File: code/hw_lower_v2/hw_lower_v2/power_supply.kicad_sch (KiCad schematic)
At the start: 0 parts

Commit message: further lower board sch work
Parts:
- added C14, C15, C18: 10u, symbol Device:C_Polarized
- added C16, C19: 100u, symbol Device:C_Polarized
- added C17: 100n 25V, symbol Device:C
- added D3, D4, D5: LED, Diode_SMD:D_0603_1608Metric, symbol Device:LED
- added PS1: HLK-5M12, Converter_ACDC:Converter_ACDC_Hi-Link_HLK-5Mxx, symbol Converter_ACDC:HLK-5M12
- added R34, R35, R36, R37: DNP, Resistor_SMD:R_0603_1608Metric, symbol Device:R
- added R38: 510, Resistor_SMD:R_0603_1608Metric, symbol Device:R
- added R39: 160, Resistor_SMD:R_0603_1608Metric, symbol Device:R
- added R40: 75, Resistor_SMD:R_0603_1608Metric, symbol Device:R
- added U5, U6: AMS1117, Package_TO_SOT_SMD:SOT-223-3_TabPin2, symbol Regulator_Linear:AMS1117
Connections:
- net L_in: now also PS1.1 (AC/L)
- net N_in: now also PS1.2 (AC/N)
- new net: D4.1 (K), R39.1
- new net: R34.1, R35.2, U5.1 (ADJ)
- new net: D3.1 (K), R38.1
- new net: D5.1 (K), R40.1
- new net: R36.1, R37.2, U6.1 (ADJ)
- new net +12V: C14.1, C15.1, C17.1, C18.1, D4.2 (A), PS1.4 (+Vout), U5.3 (VI), U6.3 (VI)
- new net +3.3V: C16.1, D5.2 (A), R34.2, U5.2 (VO)
- new net +5V: C19.1, D3.2 (A), R36.2, U6.2 (VO)
- new net GND: C14.2, C15.2, C16.2, C17.2, C18.2, C19.2, PS1.3 (-Vout), R35.1, R37.1, R38.2, R39.2, R40.2
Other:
- note added: "line overvoltage protection MOS?"

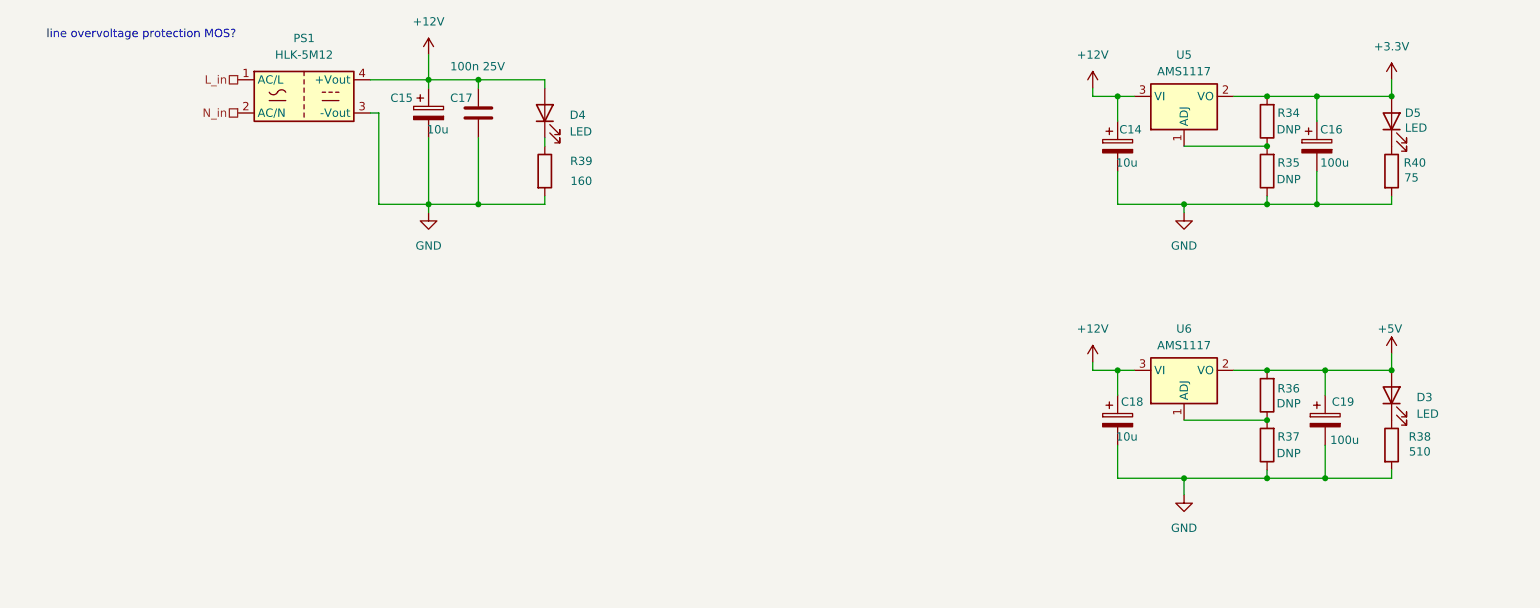
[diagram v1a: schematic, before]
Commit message: add 12V voltage inverter and polish
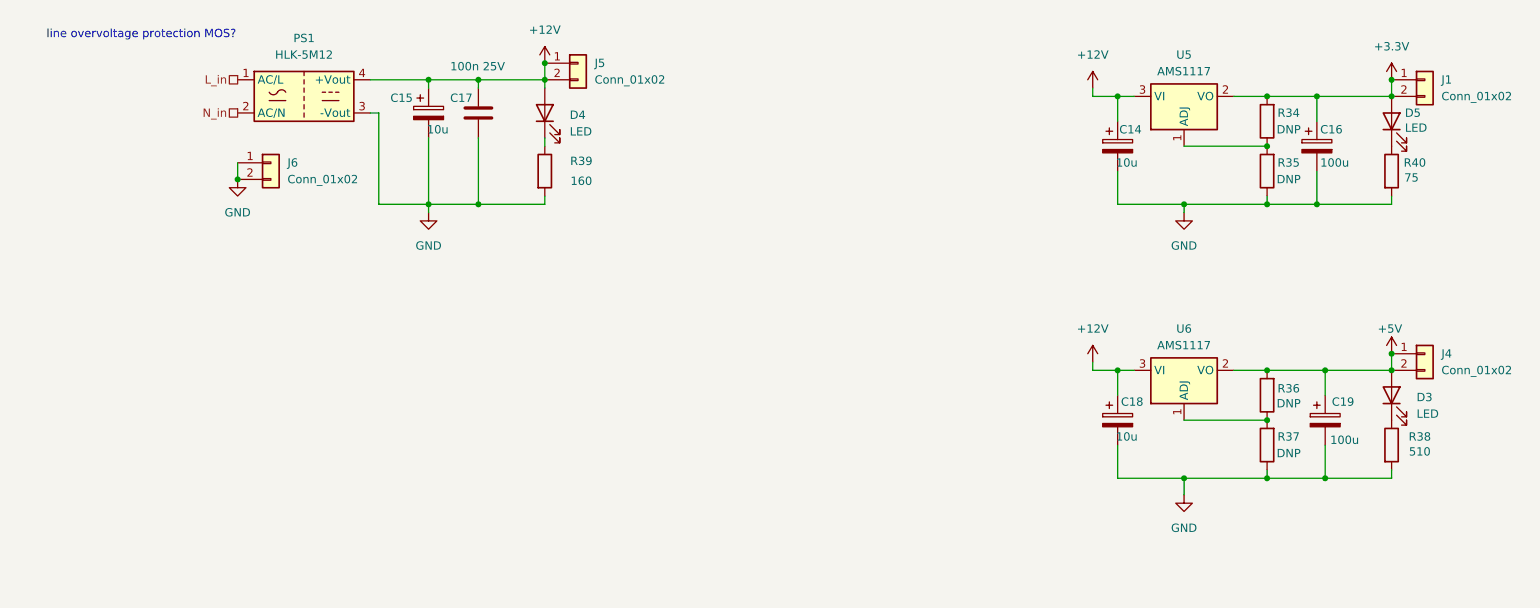
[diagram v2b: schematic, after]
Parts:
- added J1, J4, J5, J6: Conn_01x02, symbol Connector_Generic:Conn_01x02
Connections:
- net +12V: now also J5.1 (Pin_1), J5.2 (Pin_2)
- net +3.3V: now also J1.1 (Pin_1), J1.2 (Pin_2)
- net +5V: now also J4.1 (Pin_1), J4.2 (Pin_2)
- net GND: now also J6.1 (Pin_1), J6.2 (Pin_2)

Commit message: schematic is done
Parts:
- added C20, C21: 10u, symbol Device:C_Polarized
- added C9: 0.1uF/275Vac, symbol Device:C
- added F1: 1A, symbol Device:Fuse
- added FL1: Filter_EMI_CommonMode, symbol Device:Filter_EMI_CommonMode
- added J7, J8: Conn_01x02, symbol Connector_Generic:Conn_01x02
- added RV1: 10D561K, symbol Device:Varistor
- added U7: ICL7660A, symbol multi_new:ICL7660A
- C17: value 100n 25V -> 100n; footprint (none) -> Capacitor_SMD:C_0805_2012Metric
- PS1: JLCPCB Part # (none) -> C2923575
- R34: value DNP -> 75R
- R35, R37: value DNP -> 120R
- R36: value DNP -> 39R
- R38: value 510 -> 510R
- R39: value 160 -> 160R
- R40: value 75 -> 75R
- U5, U6: JLCPCB Part # (none) -> C347224
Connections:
- net +12V: now also J8.1 (Pin_1), J8.2 (Pin_2), U7.8 (V+)
- net GND: now also C21.1, U7.3 (GND)
- net L_in: now also F1.1; no longer PS1.1 (AC/L)
- net N_in: now also C9.2, FL1.3, RV1.2; no longer PS1.2 (AC/N)
- new net: C20.1, U7.2 (CAP+)
- new net: C20.2, U7.4 (CAP-)
- new net: C9.1, F1.2, FL1.1, RV1.1
- new net: FL1.2, PS1.1 (AC/L)
- new net: FL1.4, PS1.2 (AC/N)
- new net -12V: C21.2, J7.1 (Pin_1), J7.2 (Pin_2), U7.5 (VOUT)
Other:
- note removed: "line overvoltage protection MOS?"
- moved on the sheet: C15, C17, D4, J5, J6, PS1, R39

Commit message: finishing up sch and creating footprints
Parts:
- renumbered C9 to C12, C15 to C13, C17 to C14, C20 to C15, C21 to C16, C14 to C17, C16 to C19, C19 to C20, D3 to D6, J8 to J10, J5 to J11, J7 to J12, J1 to J13, J4 to J14, J6 to J9, R39 to R37, R34 to R38, R35 to R39, R36 to R40, R37 to R41, R40 to R42, R38 to R43, U7 to U5, U5 to U6, U6 to U7

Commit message: wip
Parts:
- C12: JLCPCB Part # C914484 -> (none); LCSC (none) -> C914484
- PS1: JLCPCB Part # C2923575 -> (none); LCSC (none) -> C2923575
- RV1: JLCPCB Part # C2761663 -> (none); LCSC (none) -> C2761663
- U5: JLCPCB Part # C7881 -> (none); LCSC (none) -> C7881
- U6, U7: JLCPCB Part # C347224 -> (none); LCSC (none) -> C347224

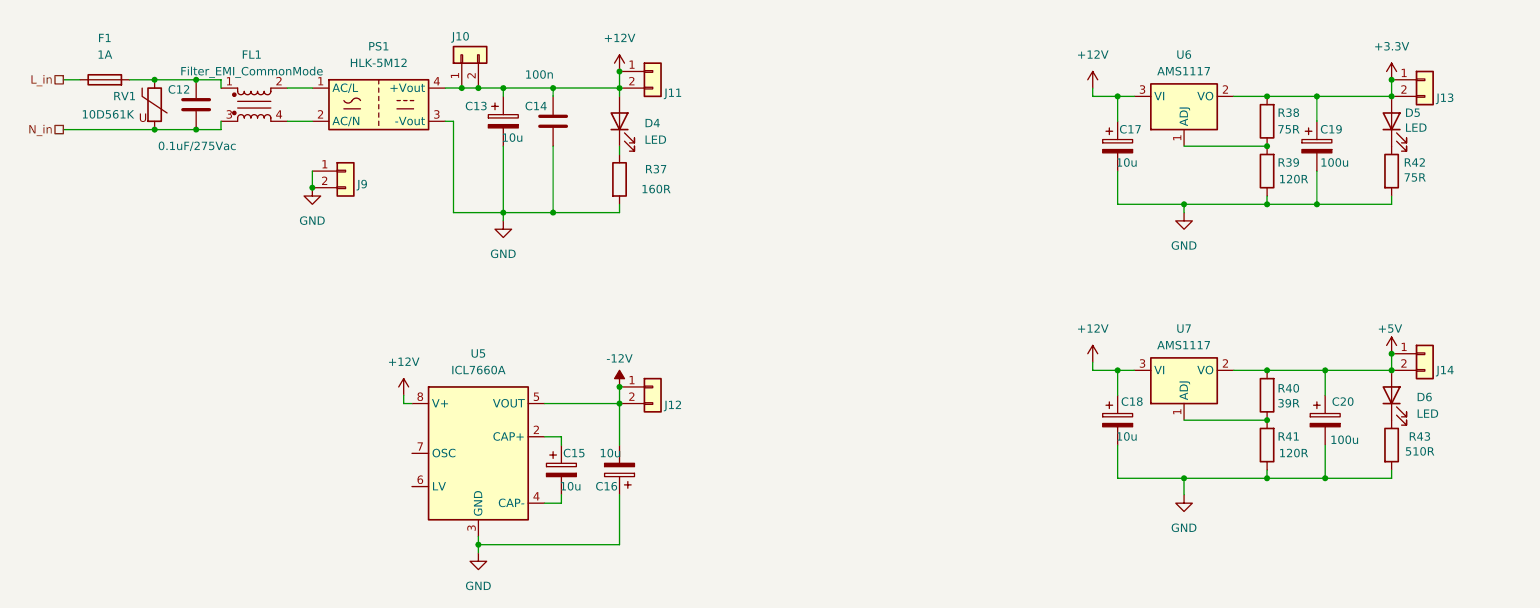
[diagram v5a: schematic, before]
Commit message: finished schematic, started first pass of layout
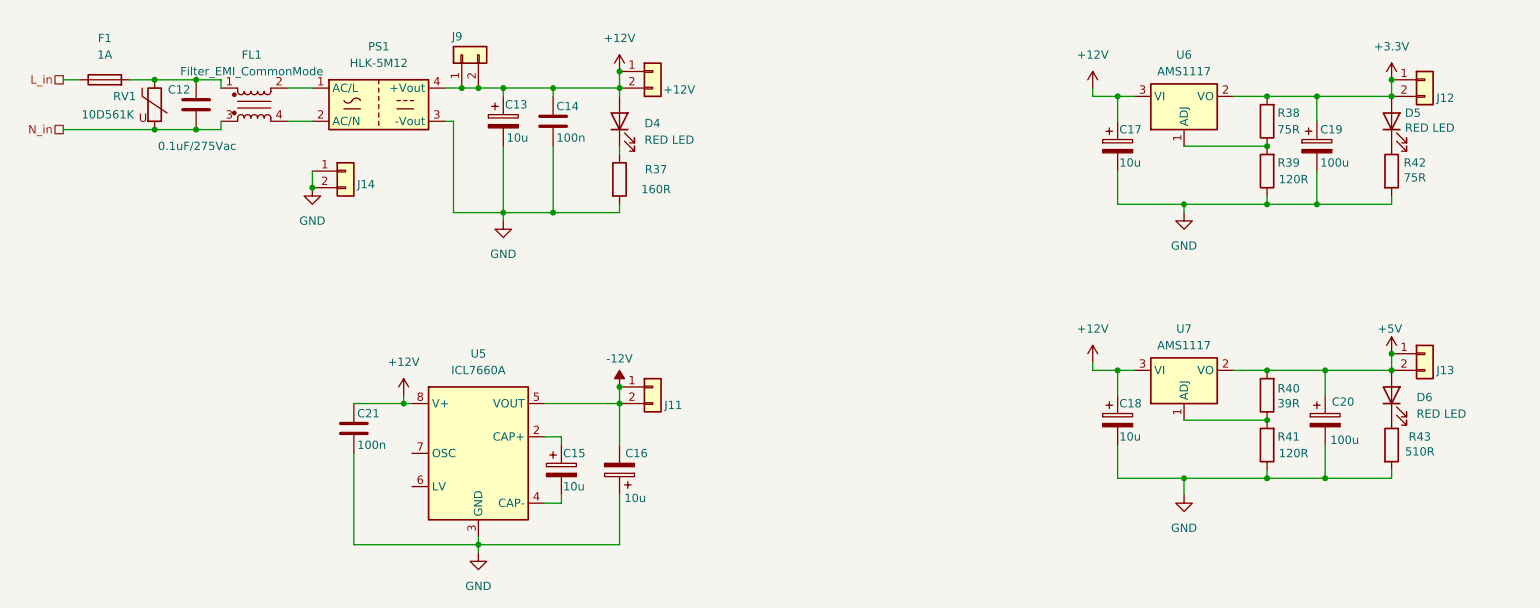
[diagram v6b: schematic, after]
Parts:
- added C21: 100n, Capacitor_SMD:C_0805_2012Metric, symbol Device:C
- C12: footprint (none) -> JLCPCB:CAP-TH_L18.0-W7.0-P15.00-D0.7
- C13, C15, C16, C17, C18: value 10u -> 10u; footprint (none) -> Capacitor_SMD:CP_Elec_4x5.4; LCSC (none) -> C72485
- C14: LCSC (none) -> C38141
- C19, C20: footprint (none) -> Capacitor_SMD:CP_Elec_6.3x5.4; LCSC (none) -> C5138965
- D4, D5, D6: value LED -> RED LED; LCSC (none) -> C7496820
- F1: footprint (none) -> JLCPCB:F1206; LCSC (none) -> C910830
- FL1: footprint (none) -> JLCPCB:FILTER-TH_4P-L17.0-W12.0-P7.00-D0.6-S8.00; LCSC (none) -> C126488
- J10: renamed from J11; footprint (none) -> Connector_PinHeader_2.54mm:PinHeader_1x02_P2.54mm_Vertical; Name (none) -> +12V
- J11: renamed from J12; footprint (none) -> Connector_PinHeader_2.54mm:PinHeader_1x02_P2.54mm_Vertical
- J12: renamed from J13; footprint (none) -> Connector_PinHeader_2.54mm:PinHeader_1x02_P2.54mm_Vertical
- J13: renamed from J14; footprint (none) -> Connector_PinHeader_2.54mm:PinHeader_1x02_P2.54mm_Vertical
- J14: renamed from J9; footprint (none) -> Connector_PinHeader_2.54mm:PinHeader_1x02_P2.54mm_Vertical
- J9: renamed from J10; footprint (none) -> Connector_PinHeader_2.54mm:PinHeader_1x02_P2.54mm_Vertical
- R37: LCSC (none) -> C22814
- R38, R42: LCSC (none) -> C112309
- R39, R41: LCSC (none) -> C125925
- R40: LCSC (none) -> C137733
- R43: LCSC (none) -> C23193
- RV1: footprint (none) -> JLCPCB:RES-TH_L12.5-W4.4-P7.50-D0.8-S3.60
- U5: footprint (none) -> JLCPCB:SOIC-8_L5.0-W4.0-P1.27-LS6.0-BL
- U6, U7: footprint Package_TO_SOT_SMD:SOT-223-3_TabPin2 -> JLCPCB:SOT-223_L6.7-W3.5-P2.30-BR
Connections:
- net +12V: now also C21.1
- net GND: now also C21.2

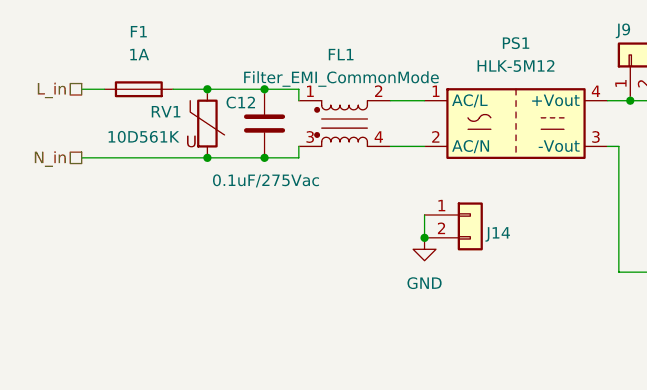
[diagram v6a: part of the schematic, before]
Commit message: Preliminary pcb component placement done
PCB size currently is around 100mm X 100mm with the mezanine board being ~40mm x 100mm
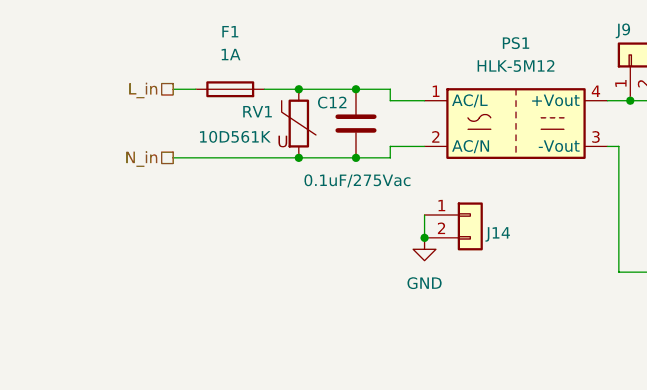
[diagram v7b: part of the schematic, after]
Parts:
- removed FL1: Filter_EMI_CommonMode, JLCPCB:FILTER-TH_4P-L17.0-W12.0-P7.00-D0.6-S8.00, symbol Device:Filter_EMI_CommonMode
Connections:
- net N_in: now also PS1.2 (AC/N)
- net at C12.1, F1.2, RV1.1: now also PS1.1 (AC/L)
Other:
- moved on the sheet: C12, F1, RV1
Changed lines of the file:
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@@
 	)
 	(junction
-		(at 54.61 39.37)
+		(at 64.77 39.37)
 		(diameter 0)
 		(color 0 0 0 0)
@@
 	)
 	(junction
-		(at 48.26 46.99)
+		(at 58.42 46.99)
 		(diameter 0)
 		(color 0 0 0 0)
 	)
 	(junction
-		(at 54.61 46.99)
+		(at 64.77 46.99)
 		(diameter 0)
 		(color 0 0 0 0)
 	)
 	(junction
-		(at 48.26 39.37)
+		(at 58.42 39.37)
 		(diameter 0)
 		(color 0 0 0 0)
@@
 	(wire
 		(pts
-			(xy 58.42 45.72) (xy 58.42 46.99)
+			(xy 68.58 45.72) (xy 68.58 46.99)
 		)
 		(stroke
@@
 	(wire
 		(pts
-			(xy 34.29 39.37) (xy 36.83 39.37)
+			(xy 44.45 39.37) (xy 46.99 39.37)
 		)
 		(stroke
@@
 	(wire
 		(pts
-			(xy 58.42 40.64) (xy 58.42 39.37)
+			(xy 68.58 40.64) (xy 68.58 39.37)
 		)
 		(stroke
@@
 	(wire
 		(pts
-			(xy 54.61 46.99) (xy 58.42 46.99)
+			(xy 64.77 46.99) (xy 68.58 46.99)
 		)
 		(stroke
@@
 	(wire
 		(pts
-			(xy 48.26 46.99) (xy 54.61 46.99)
+			(xy 58.42 46.99) (xy 64.77 46.99)
 		)
 		(stroke
@@
 	(wire
 		(pts
-			(xy 44.45 39.37) (xy 48.26 39.37)
+			(xy 54.61 39.37) (xy 58.42 39.37)
 		)
 		(stroke
@@
 	(wire
 		(pts
-			(xy 34.29 46.99) (xy 48.26 46.99)
+			(xy 44.45 46.99) (xy 58.42 46.99)
 		)
 		(stroke
@@
 	(wire
 		(pts
-			(xy 54.61 39.37) (xy 58.42 39.37)
+			(xy 64.77 39.37) (xy 68.58 39.37)
 		)
 		(stroke
@@
 	(wire
 		(pts
-			(xy 48.26 39.37) (xy 54.61 39.37)
+			(xy 58.42 39.37) (xy 64.77 39.37)
 		)
 		(stroke
@@
 	(hierarchical_label "N_in"
 		(shape passive)
-		(at 34.29 46.99 180)
+		(at 44.45 46.99 180)
 		(fields_autoplaced yes)
 		(effects
@@
 	(hierarchical_label "L_in"
 		(shape passive)
-		(at 34.29 39.37 180)
+		(at 44.45 39.37 180)
 		(fields_autoplaced yes)
 		(effects
@@
 	(symbol
 		(lib_id "Device:C")
-		(at 54.61 43.18 0)
+		(at 64.77 43.18 0)
 		(unit 1)
 		(exclude_from_sim no)
@@
 		(dnp no)
 		(property "Reference" "C12"
-			(at 50.292 40.894 0)
+			(at 60.452 40.894 0)
 			(effects
 				(font
@@
 		)
 		(property "Value" "0.1uF/275Vac"
-			(at 48.768 49.53 0)
+			(at 58.928 49.53 0)
 			(effects
 				(font
@@
 		)
 		(property "Footprint" "JLCPCB:CAP-TH_L18.0-W7.0-P15.00-D0.7"
-			(at 55.5752 46.99 0)
+			(at 65.7352 46.99 0)
 			(effects
 				(font
@@
 		)
 		(property "Datasheet" "~"
-			(at 54.61 43.18 0)
+			(at 64.77 43.18 0)
 			(effects
 				(font
@@
 		)
 		(property "Description" "Unpolarized capacitor"
-			(at 54.61 43.18 0)
+			(at 64.77 43.18 0)
 			(effects
 				(font
@@
 		)
 		(property "LCSC" "C914484"
-			(at 54.61 43.18 0)
+			(at 64.77 43.18 0)
 			(effects
 				(font
@@
 	(symbol
 		(lib_id "Device:Fuse")
-		(at 40.64 39.37 90)
+		(at 50.8 39.37 90)
 		(unit 1)
 		(exclude_from_sim no)
@@
 		(fields_autoplaced yes)
 		(property "Reference" "F1"
-			(at 40.64 33.02 90)
+			(at 50.8 33.02 90)
 			(effects
 				(font
@@
 		)
 		(property "Value" "1A"
-			(at 40.64 35.56 90)
+			(at 50.8 35.56 90)
 			(effects
 				(font
@@
 		)
 		(property "Footprint" "JLCPCB:F1206"
-			(at 40.64 41.148 90)
+			(at 50.8 41.148 90)
 			(effects
 				(font
@@
 		)
 		(property "Datasheet" "~"
-			(at 40.64 39.37 0)
+			(at 50.8 39.37 0)
 			(effects
 				(font
@@
 		)
 		(property "Description" "Fuse"
-			(at 40.64 39.37 0)
+			(at 50.8 39.37 0)
 			(effects
 				(font
@@
 		)
 		(property "LCSC" "C910830"
-			(at 40.64 39.37 0)
+			(at 50.8 39.37 0)
 			(effects
 				(font
@@
 	(symbol
 		(lib_id "Device:Varistor")
-		(at 48.26 43.18 0)
+		(at 58.42 43.18 0)
 		(unit 1)
 		(exclude_from_sim no)
@@
 		(dnp no)
 		(property "Reference" "RV1"
-			(at 41.91 41.91 0)
+			(at 52.07 41.91 0)
 			(effects
 				(font
@@
 		)
 		(property "Value" "10D561K"
-			(at 37.084 44.704 0)
+			(at 47.244 44.704 0)
 			(effects
 				(font
@@
 		)
 		(property "Footprint" "JLCPCB:RES-TH_L12.5-W4.4-P7.50-D0.8-S3.60"
-			(at 46.482 43.18 90)
+			(at 56.642 43.18 90)
 			(effects
 				(font
@@
 		)
 		(property "Datasheet" "~"
-			(at 48.26 43.18 0)
+			(at 58.42 43.18 0)
 			(effects
 				(font
@@
 		)
 		(property "Description" "Voltage dependent resistor"
-			(at 48.26 43.18 0)
+			(at 58.42 43.18 0)
 			(effects
 				(font
@@
 		)
 		(property "Sim.Name" "kicad_builtin_varistor"
-			(at 48.26 43.18 0)
+			(at 58.42 43.18 0)
 			(effects
 				(font
@@
 		)
 		(property "Sim.Device" "SUBCKT"
-			(at 48.26 43.18 0)
+			(at 58.42 43.18 0)
 			(effects
 				(font
@@
 		)
 		(property "Sim.Pins" "1=A 2=B"
-			(at 48.26 43.18 0)
+			(at 58.42 43.18 0)
 			(effects
 				(font
@@
 		)
 		(property "Sim.Params" "threshold=1k"
-			(at 48.26 43.18 0)
+			(at 58.42 43.18 0)
 			(effects
 				(font
@@
 		)
 		(property "Sim.Library" "${KICAD7_SYMBOL_DIR}/Simulation_SPICE.sp"
-			(at 48.26 43.18 0)
+			(at 58.42 43.18 0)
 			(effects
 				(font
@@
 		)
 		(property "LCSC" "C2761663"
-			(at 48.26 43.18 0)
+			(at 58.42 43.18 0)
 			(effects
 				(font
@@
 					(unit 1)
 				)
-			)
-		)
-	)
-	(symbol
-		(lib_id "Device:Filter_EMI_CommonMode")
-		(at 63.5 43.18 0)
-		(unit 1)
-		(exclude_from_sim no)
-		(in_bom yes)
-		(on_board yes)
-		(dnp no)
-		(fields_autoplaced yes)
-		(property "Reference" "FL1"
-			(at 63.119 35.56 0)
-			(effects
-				(font
-					(size 1.27 1.27)
-				)
-			)
-		)
-		(property "Value" "Filter_EMI_CommonMode"
-			(at 63.119 38.1 0)
-			(effects
-				(font
-					(size 1.27 1.27)
-				)
-			)
-		)
-		(property "Footprint" "JLCPCB:FILTER-TH_4P-L17.0-W12.0-P7.00-D0.6-S8.00"
-			(at 63.5 42.164 0)
-			(effects
-				(font
-					(size 1.27 1.27)
-				)
-				(hide yes)
-			)
-		)
-		(property "Datasheet" "~"
-			(at 63.5 42.164 0)
-			(effects
-				(font
-					(size 1.27 1.27)
-				)
-				(hide yes)
-			)
-		)
-		(property "Description" "EMI 2-inductor common mode filter"
-			(at 63.5 43.18 0)
-			(effects
-				(font
-					(size 1.27 1.27)
-				)
-				(hide yes)
-			)
-		)
-		(property "LCSC" "C126488"
-			(at 63.5 43.18 0)
-			(effects
-				(font
-					(size 1.27 1.27)
-				)
-				(hide yes)
-			)
-		)
-		(pin "3"
-		)
-		(pin "2"
-		)
-		(pin "1"
-		)
-		(pin "4"
-		)
-		(instances
-			(project ""
-				(path "/c5175f1c-553a-46da-abbd-483c59ad8dfa/20fd194e-5497-4849-a679-c90ed918333e"
-					(reference "FL1")
-					(unit 1)
-				)
